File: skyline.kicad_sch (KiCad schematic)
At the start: 0 parts

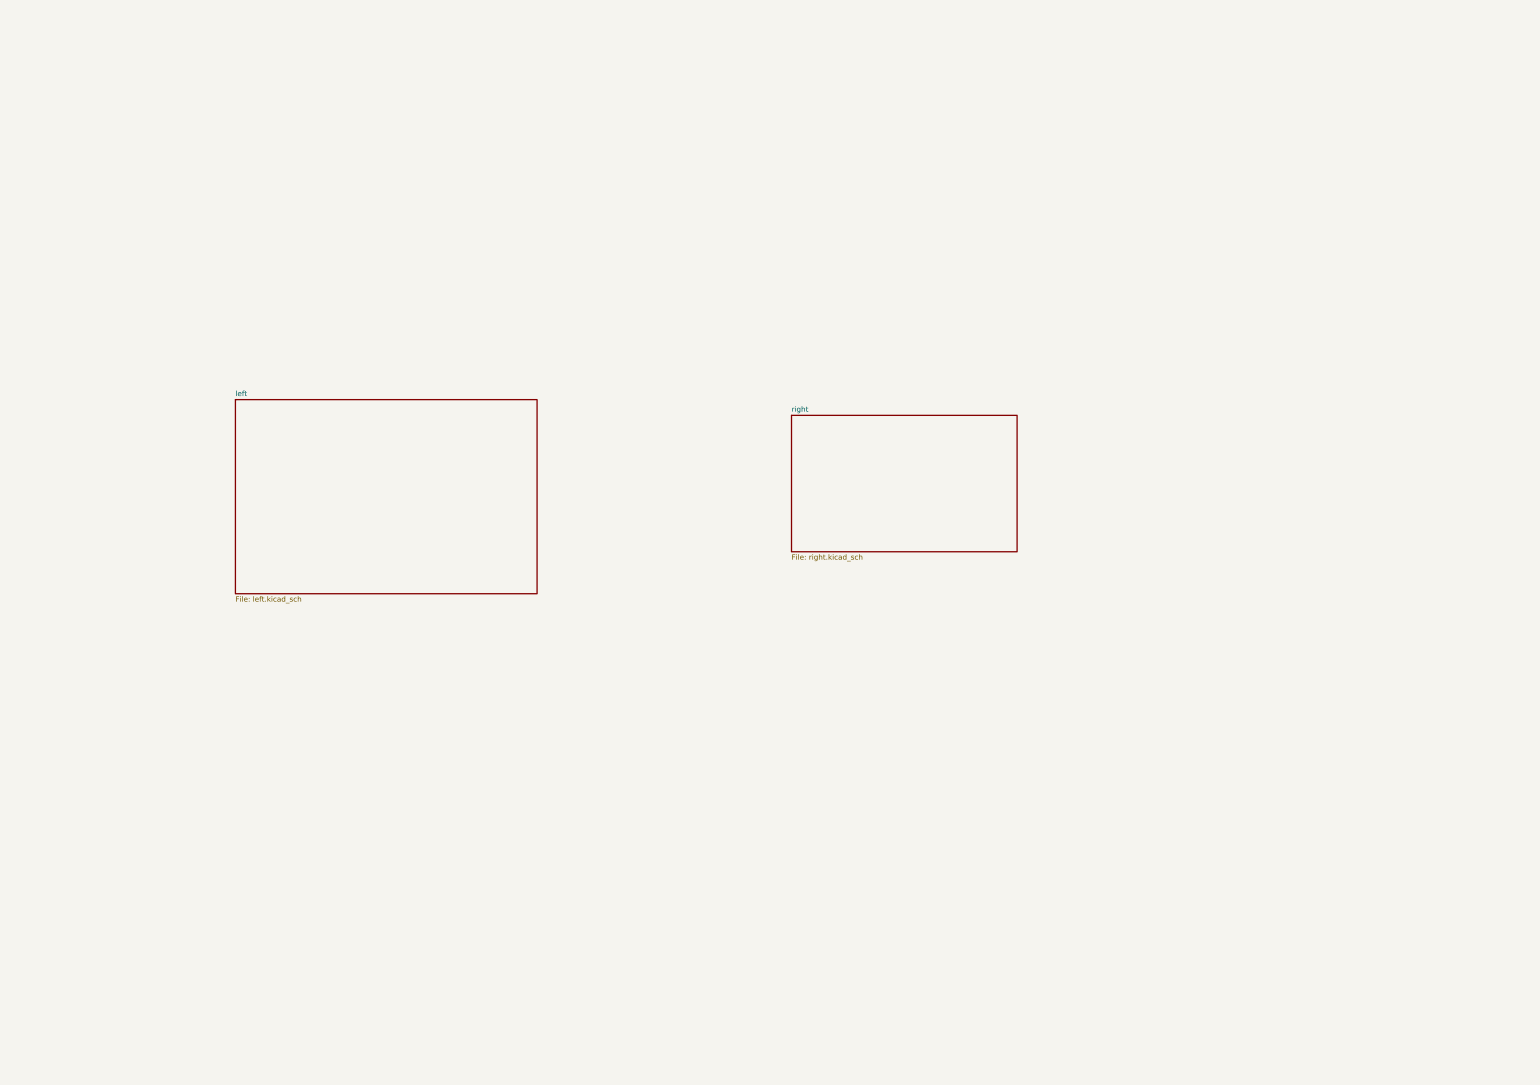
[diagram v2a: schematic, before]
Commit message: deleted left and right schematics, just main now
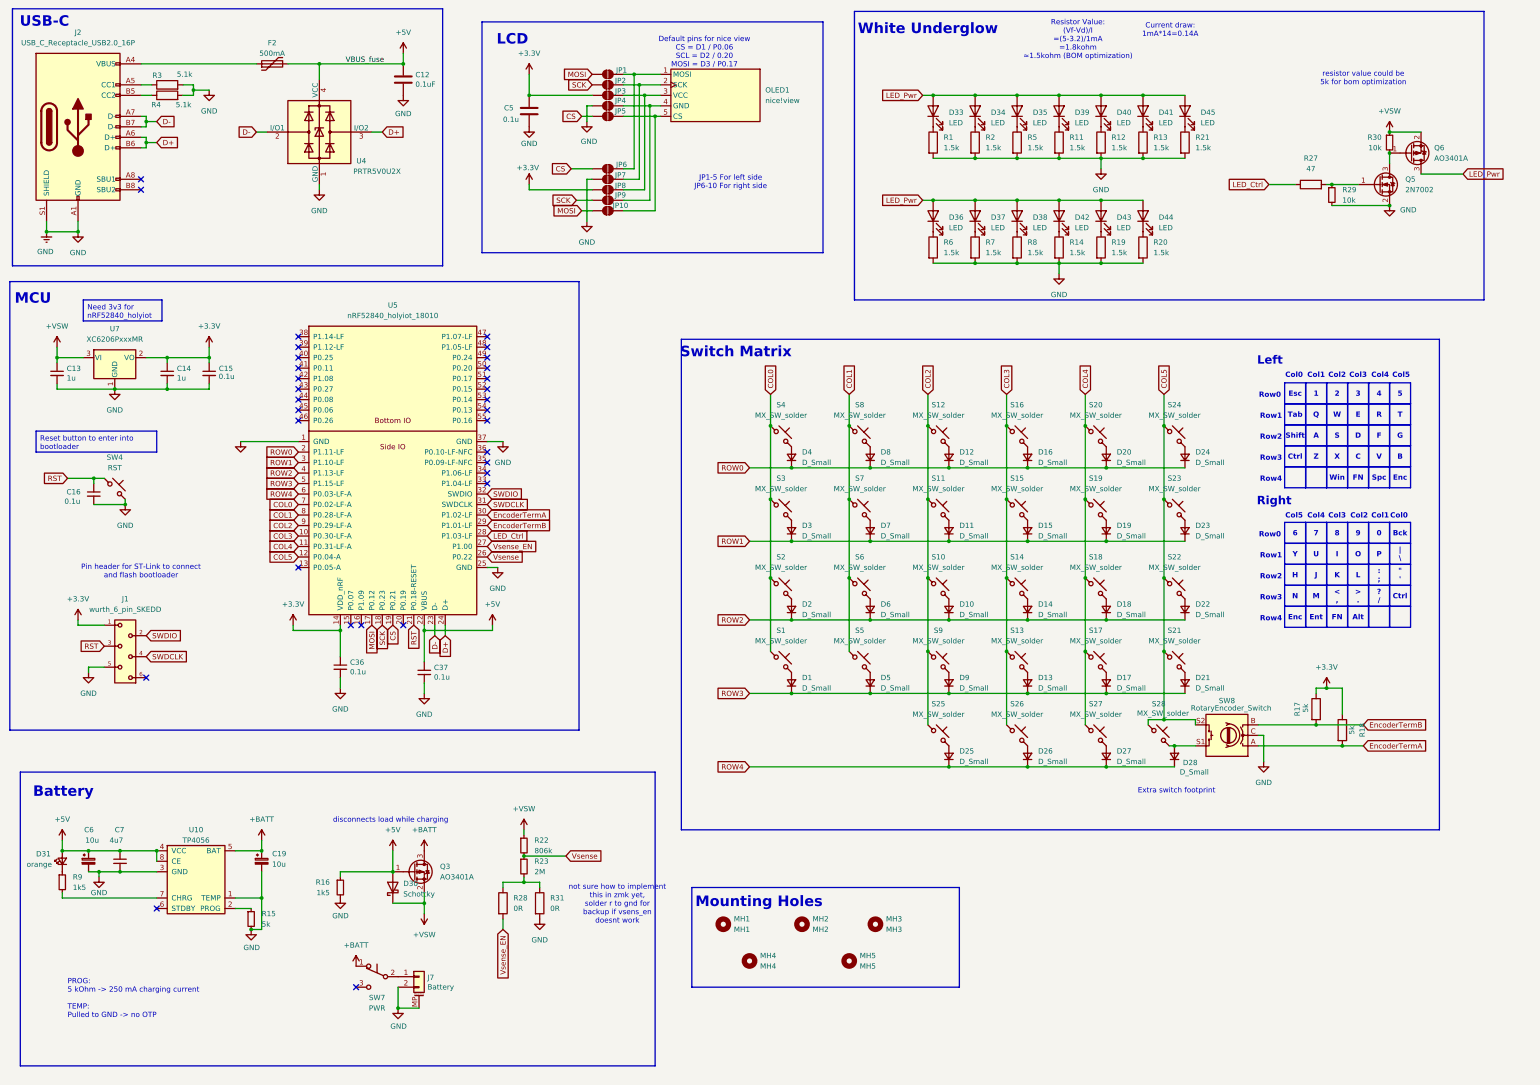
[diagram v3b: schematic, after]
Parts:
- added C12: 0.1uF, Capacitor_SMD:C_0805_2012Metric_Pad1.18x1.45mm_HandSolder, symbol Device:C
- added C13, C14: 1u, Capacitor_SMD:C_0805_2012Metric_Pad1.18x1.45mm_HandSolder, symbol Device:C_Small
- added C15, C16, C36, C37: 0.1u, Capacitor_SMD:C_0805_2012Metric_Pad1.18x1.45mm_HandSolder, symbol Device:C_Small
- added C19, C6: 10u, Capacitor_Tantalum_SMD:CP_EIA-3216-18_Kemet-A_Pad1.58x1.35mm_HandSolder, symbol Device:C_Polarized_Small
- added C5: 0.1u, Capacitor_SMD:C_0805_2012Metric_Pad1.18x1.45mm_HandSolder, symbol Device:C
- added C7: 4u7, Capacitor_SMD:C_0805_2012Metric_Pad1.18x1.45mm_HandSolder, symbol Device:C_Small
- added D1, D10, D11, D12, D13, D14, D15, D16, D17, D18, D19, D2, D20, D21, D22, D23, D24, D25, D26, D27, D28, D3, D4, D5, D6, D7, D8, D9: D_Small, Diode_SMD:D_0805_2012Metric_Pad1.15x1.40mm_HandSolder, symbol Device:D_Small
- added D30: Schottky, Diode_SMD:D_SOD-123, symbol Device:D_Schottky
- added D31: orange, LED_SMD:LED_0402_1005Metric_Pad0.77x0.64mm_HandSolder, symbol Device:LED_Small
- added D33, D34, D35, D36, D37, D38, D39, D40, D41, D42, D43, D44, D45: LED, reversible_skyline:reversible_D_0805_2012Metric_Pad1.15x1.40mm_HandSolder, symbol Device:LED
- added F2: 500mA, Fuse:Fuse_1206_3216Metric, symbol Device:Polyfuse
- added J1: wurth_6_pin_SKEDD, 490107670612:wurth_6_pin_SKEDD, symbol Wurth_6_pin_Connector:wurth_6_pin_SKEDD
- added J2: USB_C_Receptacle_USB2.0_16P, reversible_skyline:USB_C_Receptacle_HRO_TYPE-C-31-M-12_reversible, symbol Connector:USB_C_Receptacle_USB2.0_16P
- added J7: Battery, reversible_skyline:reversible_Molex_Pico-EZmate_78171-0002_1x02-1MP_P1.20mm_Vertical, symbol Connector_Generic_MountingPin:Conn_01x02_MountingPin
- added JP1, JP10, JP2, JP3, JP4, JP5, JP6, JP7, JP8, JP9: SolderJumper_2_Open, reversible_skyline:Jumper_solder, symbol Jumper:SolderJumper_2_Open
- added MH1: MH1, reversible_skyline:mounting_hole_npth, symbol Mechanical:MountingHole
- added MH2: MH2, reversible_skyline:mounting_hole_npth, symbol Mechanical:MountingHole
- added MH3: MH3, reversible_skyline:mounting_hole_npth, symbol Mechanical:MountingHole
- added MH4: MH4, reversible_skyline:mounting_hole_npth, symbol Mechanical:MountingHole
- added MH5: MH5, reversible_skyline:mounting_hole_npth, symbol Mechanical:MountingHole
- added OLED1: nice!view, nice_view:nice_view, symbol nice_view:nice!view
- added Q3, Q6: AO3401A, Package_TO_SOT_SMD:SOT-23, symbol Transistor_FET:AO3401A
- added Q5: 2N7002, Package_TO_SOT_SMD:SOT-23, symbol Transistor_FET:2N7002
- added R1, R11, R12, R13, R14, R19, R2, R20, R21, R5, R6, R7, R8: 1.5k, Resistor_SMD:R_0805_2012Metric_Pad1.20x1.40mm_HandSolder, symbol Device:R
- added R15: 5k, Resistor_SMD:R_0805_2012Metric_Pad1.20x1.40mm_HandSolder, symbol Device:R_Small
- added R16, R9: 1k5, Resistor_SMD:R_0805_2012Metric_Pad1.20x1.40mm_HandSolder, symbol Device:R_Small
- added R17, R18: 5k, Resistor_SMD:R_0805_2012Metric_Pad1.20x1.40mm_HandSolder, symbol Device:R
- added R22: 806k, Resistor_SMD:R_0805_2012Metric_Pad1.20x1.40mm_HandSolder, symbol Device:R_Small
- added R23: 2M, Resistor_SMD:R_0805_2012Metric_Pad1.20x1.40mm_HandSolder, symbol Device:R_Small
- added R27: 47, Resistor_SMD:R_0805_2012Metric_Pad1.20x1.40mm_HandSolder, symbol Device:R
- added R28, R31: 0R, Resistor_SMD:R_0805_2012Metric_Pad1.20x1.40mm_HandSolder, symbol Device:R
- added R29, R30: 10k, Resistor_SMD:R_0805_2012Metric_Pad1.20x1.40mm_HandSolder, symbol Device:R_Small
- added R3, R4: 5.1k, Resistor_SMD:R_0805_2012Metric_Pad1.20x1.40mm_HandSolder, symbol Device:R
- added S1, S10, S11, S12, S13, S14, S15, S16, S17, S18, S19, S2, S20, S21, S22, S23, S24, S25, S26, S27, S28, S3, S4, S5, S6, S7, S8, S9: MX_SW_solder, PCM_marbastlib-xp-mx:SW_MX_Reversible_1u, symbol PCM_marbastlib-mx:MX_SW_solder
- added SW4: RST, reversible_skyline:reversible_SW_SPST_SKQG_WithStem, symbol Switch:SW_Push_45deg
- added SW7: PWR, PCM_marbastlib-various:reversible_SW_MSK12C02-HB, symbol Switch:SW_Push_SPDT
- added SW8: RotaryEncoder_Switch, PCM_marbastlib-various:ROT_Alps_EC11E-Switch, symbol Device:RotaryEncoder_Switch
- added U10: TP4056, Package_SO:SOP-8-1EP_4.57x4.57mm_P1.27mm_EP4.57x4.45mm, symbol PCM_marbastlib-various:TP4056
- added U4: PRTR5V0U2X, Package_TO_SOT_SMD:SOT-143, symbol Power_Protection:PRTR5V0U2X
- added U5: nRF52840_holyiot_18010, reversible_skyline:nRF52840_holyiot_18010_HS_simple_reversible, symbol PCM_marbastlib-various:nRF52840_holyiot_18010
- added U7: XC6206PxxxMR, Package_TO_SOT_SMD:SOT-23, symbol Regulator_Linear:XC6206PxxxMR
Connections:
- new net: D10.2 (A), S10.2
- new net: D27.2 (A), S27.2
- new net: D44.1 (K), R20.1
- new net: J7.1 (Pin_1), SW7.2 (B)
- new net: R23.2, R28.1, R31.1
- new net: D14.2 (A), S14.2
- new net: D22.2 (A), S22.2
- new net: D15.2 (A), S15.2
- new net: D42.1 (K), R14.1
- new net: D13.2 (A), S13.2
- new net: D33.1 (K), R1.1
- new net: D43.1 (K), R19.1
- new net: F2.1, J2.A4 (VBUS), J2.A9 (VBUS), J2.B4 (VBUS), J2.B9 (VBUS)
- new net: J2.A5 (CC1), R3.1
- new net: J2.B5 (CC2), R4.1
- new net: D28.2 (A), S28.2, SW8.S1
- new net: JP4.2 (B), JP9.2 (B), OLED1.4 (GND)
- new net: D4.2 (A), S4.2
- new net: D6.2 (A), S6.2
- new net: JP1.2 (B), JP6.2 (B), OLED1.1 (MOSI)
- new net: JP10.2 (B), JP5.2 (B), OLED1.5 (CS)
- new net: D38.1 (K), R8.1
- new net: D12.2 (A), S12.2
- new net: D9.2 (A), S9.2
- new net: JP2.2 (B), JP7.2 (B), OLED1.2 (SCK)
- new net: JP3.2 (B), JP8.2 (B), OLED1.3 (VCC)
- new net: D34.1 (K), R2.1
- new net: D5.2 (A), S5.2
- new net: D31.1 (K), R9.1
- new net: D3.2 (A), S3.2
- new net: D20.2 (A), S20.2
- new net: Q5.3 (D), Q6.1 (G), R30.2
- new net: D26.2 (A), S26.2
- new net: D7.2 (A), S7.2
- new net: D24.2 (A), S24.2
- new net: Q5.1 (G), R27.2, R29.1
- new net: D25.2 (A), S25.2
- new net: D18.2 (A), S18.2
- new net: D17.2 (A), S17.2
- new net: D36.1 (K), R6.1
- new net: D41.1 (K), R13.1
- new net: D37.1 (K), R7.1
- new net: D21.2 (A), S21.2
- new net: D23.2 (A), S23.2
- new net: R15.1, U10.2 (PROG)
- new net: R9.2, U10.7 (CHRG)
- new net: D11.2 (A), S11.2
- new net: D39.1 (K), R11.1
- new net: D35.1 (K), R5.1
- new net: D1.2 (A), S1.2
- new net: D8.2 (A), S8.2
- new net: D16.2 (A), S16.2
- new net: D19.2 (A), S19.2
- new net: D40.1 (K), R12.1
- new net: D2.2 (A), S2.2
- new net: D45.1 (K), R21.1
- new net +3.3V: C14.1, C15.1, C36.1, C5.1, J1.1, JP3.1 (A), JP8.1 (A), R17.1, R18.1, U5.14 (VDD_nRF), U7.2 (VO)
- new net +5V: C12.1, C37.1, C6.1, C7.1, D30.2 (A), D31.2 (A), F2.2, Q3.1 (G), R16.1, U10.4 (VCC), U10.8 (CE), U4.4 (VCC), U5.22 (VBUS)
- new net +BATT: C19.1, Q3.3 (D), SW7.1 (A), U10.5 (BAT)
- new net +VSW: C13.1, D30.1 (K), Q3.2 (S), Q6.2 (S), R22.1, R30.1, U7.3 (VI)
- new net COL0: S1.1, S2.1, S3.1, S4.1, U5.7 (P0.02-LF-A)
- new net COL1: S5.1, S6.1, S7.1, S8.1, U5.8 (P0.28-LF-A)
- new net COL2: S10.1, S11.1, S12.1, S25.1, S9.1, U5.9 (P0.29-LF-A)
- new net COL3: S13.1, S14.1, S15.1, S16.1, S26.1, U5.10 (P0.30-LF-A)
- new net COL4: S17.1, S18.1, S19.1, S20.1, S27.1, U5.11 (P0.31-LF-A)
- new net COL5: S21.1, S22.1, S23.1, S24.1, S28.1, SW8.S2, U5.12 (P0.04-A)
- new net CS: JP5.1 (A), JP6.1 (A), U5.19 (P0.21)
- new net D+: J2.A6 (D+), J2.B6 (D+), U4.3 (I/O2), U5.24 (D+)
- new net D-: J2.A7 (D-), J2.B7 (D-), U4.2 (I/O1), U5.23 (D-)
- new net EncoderTermA: R18.2, SW8.A, U5.30 (P1.02-LF)
- new net EncoderTermB: R17.2, SW8.B, U5.29 (P1.01-LF)
- new net GND: C12.2, C13.2, C14.2, C15.2, C16.2, C19.2, C36.2, C37.2, C5.2, C6.2, C7.2, J1.5, J2.A1 (GND), J2.A12 (GND), J2.B1 (GND), J2.B12 (GND), J2.S1 (SHIELD), J7.2 (Pin_2), J7.MP (MountPin), JP4.1 (A), JP7.1 (A), Q5.2 (S), R1.2, R11.2, R12.2, R13.2, R14.2, R15.2, R16.2, R19.2, R2.2, R20.2, R21.2, R29.2, R3.2, R31.2, R4.2, R5.2, R6.2, R7.2, R8.2, SW4.2, SW8.C, U10.1 (TEMP), U10.3 (GND), U4.1 (GND), U5.1 (GND), U5.25 (GND), U5.37 (GND), U7.1 (GND)
- new net LED_Ctrl: R27.1, U5.28 (P1.03-LF)
- new net LED_Pwr: D33.2 (A), D34.2 (A), D35.2 (A), D36.2 (A), D37.2 (A), D38.2 (A), D39.2 (A), D40.2 (A), D41.2 (A), D42.2 (A), D43.2 (A), D44.2 (A), D45.2 (A), Q6.3 (D)
- new net MOSI: JP1.1 (A), JP10.1 (A), U5.17 (P0.12)
- new net ROW0: D12.1 (K), D16.1 (K), D20.1 (K), D24.1 (K), D4.1 (K), D8.1 (K), U5.2 (P1.11-LF)
- new net ROW1: D11.1 (K), D15.1 (K), D19.1 (K), D23.1 (K), D3.1 (K), D7.1 (K), U5.3 (P1.10-LF)
- new net ROW2: D10.1 (K), D14.1 (K), D18.1 (K), D2.1 (K), D22.1 (K), D6.1 (K), U5.4 (P1.13-LF)
- new net ROW3: D1.1 (K), D13.1 (K), D17.1 (K), D21.1 (K), D5.1 (K), D9.1 (K), U5.5 (P1.15-LF)
- new net ROW4: D25.1 (K), D26.1 (K), D27.1 (K), D28.1 (K), U5.6 (P0.03-LF-A)
- new net RST: C16.1, J1.3, SW4.1, U5.21 (P0.18-RESET)
- new net SCK: JP2.1 (A), JP9.1 (A), U5.18 (P0.23)
- new net SWDCLK: J1.4, U5.31 (SWDCLK)
- new net SWDIO: J1.2, U5.32 (SWDIO)
- new net Vsense: R22.2, R23.1, U5.26 (P0.22)
- new net Vsense_EN: R28.2, U5.27 (P1.00)
- no-connect marks 0 -> 31
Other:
- removed sheet left
- removed sheet right
- note added: "" '"
- note added: "0"
- note added: "1"
- note added: "2"
- note added: "3"
- note added: "4"
- note added: "5"
- note added: "6"
- note added: "7"
- note added: "8"
- note added: "9"
- note added: ": ;"
- note added: "< ,"
- note added: "> ."
- note added: "? /"
- note added: "A"
- note added: "Alt"
- note added: "B"
- note added: "Battery"
- note added: "Bck"
- note added: "C"
- note added: "Col0"
- note added: "Col1"
- note added: "Col2"
- note added: "Col3"
- note added: "Col4"
- note added: "Col5"
- note added: "Ctrl"
- note added: "Current draw: 1mA*14=0.14A"
- note added: "D"
- note added: "Default pins for nice view CS = D1 / P0.06 SCL = D2 / 0.20 MOSI = D3 / P0.17"
- note added: "E"
- note added: "Enc"
- note added: "Ent"
- note added: "Esc"
- note added: "Extra switch footprint"
- note added: "F"
- note added: "FN"
- note added: "G"
- note added: "H"
- note added: "I"
- note added: "J"
- note added: "JP1-5 For left side JP6-10 For right side"
- note added: "K"
- note added: "L"
- note added: "LCD"
- note added: "Left"
- note added: "M"
- note added: "MCU"
- note added: "Mounting Holes"
- note added: "N"
- note added: "O"
- note added: "P"
- note added: "PROG: 5 kOhm -> 250 mA charging current TEMP: Pulled to GND -> no OTP"
- note added: "Pin header for ST-Link to connect and flash bootloader"
- note added: "Q"
- note added: "R"
- note added: "Resistor Value: (Vf-Vd)/I =(5-3.2)/1mA =1.8kohm ≈1.5kohm (BOM optimization)"
- note added: "Right"
- note added: "Row0"
- note added: "Row1"
- note added: "Row2"
- note added: "Row3"
- note added: "Row4"
- note added: "S"
- note added: "Shift"
- note added: "Spc"
- note added: "Switch Matrix"
- note added: "T"
- note added: "Tab"
- note added: "U"
- note added: "USB-C"
- note added: "V"
- note added: "W"
- note added: "White Underglow"
- note added: "Win"
- note added: "X"
- note added: "Y"
- note added: "Z"
- note added: "disconnects load while charging"
- note added: "not sure how to implement this in zmk yet, solder r to gnd for backup if vsens_en doesnt work"
- note added: "resistor value could be 5k for bom optimization"
- note added: "| \"
